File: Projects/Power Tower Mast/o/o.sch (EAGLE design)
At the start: 29 parts

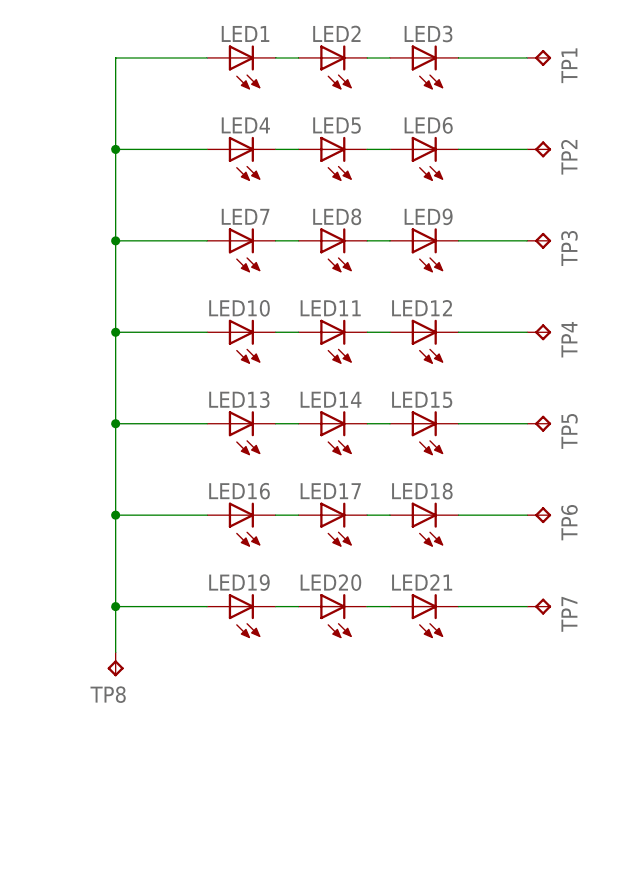
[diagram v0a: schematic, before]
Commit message: updated with extra vias and panelized
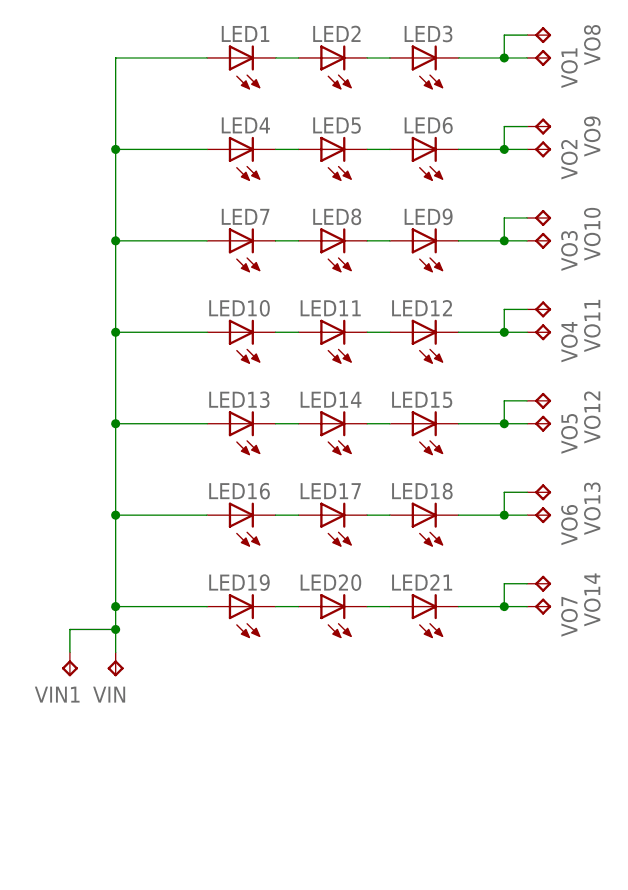
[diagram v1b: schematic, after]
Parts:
- added VIN1, VO10, VO11, VO12, VO13, VO14, VO8, VO9: (no value), CyberRailGuru:TEST_POINTPAD1-20
- renumbered TP1 to VO1, TP2 to VO2, TP3 to VO3, TP4 to VO4, TP5 to VO5, TP6 to VO6, TP7 to VO7, TP8 to VIN
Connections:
- removed net VIN2: LED1.A, LED10.A, LED13.A, LED16.A, LED19.A, LED4.A, LED7.A, VIN.TP
- removed net VOUT10: LED12.C, VO4.TP
- removed net VOUT11: LED15.C, VO5.TP
- removed net VOUT12: LED18.C, VO6.TP
- removed net VOUT13: LED21.C, VO7.TP
- removed net VOUT8: LED6.C, VO2.TP
- removed net VOUT9: LED9.C, VO3.TP
- new net VIN: LED1.A, LED10.A, LED13.A, LED16.A, LED19.A, LED4.A, LED7.A, VIN.TP, VIN1.TP
- new net VOUT1: LED3.C, VO1.TP, VO8.TP
- new net VOUT2: LED6.C, VO2.TP, VO9.TP
- new net VOUT3: LED9.C, VO10.TP, VO3.TP
- new net VOUT4: LED12.C, VO11.TP, VO4.TP
- new net VOUT5: LED15.C, VO12.TP, VO5.TP
- new net VOUT6: LED18.C, VO13.TP, VO6.TP
- net VOUT7: now also LED21.C, VO14.TP, VO7.TP; no longer LED3.C, VO1.TP

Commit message: fixed ratio for all letters; continued to update layouts
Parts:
- added LED22, LED23, LED24: (no value), CyberRailGuru:LED0805
- added VO15, VO16: (no value), CyberRailGuru:TEST_POINTPAD1-20
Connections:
- new net N$1: LED22.C, LED23.A
- new net N$2: LED23.C, LED24.A
- new net N$5: LED24.C, VO16.TP, VO8.TP
- net VIN: now also LED22.A
- net VOUT1: now also VO9.TP; no longer VO8.TP
- net VOUT2: now also VO10.TP; no longer VO9.TP
- net VOUT3: now also VO11.TP; no longer VO10.TP
- net VOUT4: now also VO12.TP; no longer VO11.TP
- net VOUT5: now also VO13.TP; no longer VO12.TP
- net VOUT6: now also VO14.TP; no longer VO13.TP
- net VOUT7: now also VO15.TP; no longer VO14.TP
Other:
- moved on the sheet: VIN, VIN1, VO10, VO11, VO12, VO13, VO14, VO8, VO9
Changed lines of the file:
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@@
 <part name="VO7" library="CyberRailGuru" deviceset="TEST_POINT" device="PAD1-20"/>
 <part name="VIN1" library="CyberRailGuru" deviceset="TEST_POINT" device="PAD1-20"/>
-<part name="VO8" library="CyberRailGuru" deviceset="TEST_POINT" device="PAD1-20"/>
 <part name="VO9" library="CyberRailGuru" deviceset="TEST_POINT" device="PAD1-20"/>
 <part name="VO10" library="CyberRailGuru" deviceset="TEST_POINT" device="PAD1-20"/>
@@
 <part name="VO13" library="CyberRailGuru" deviceset="TEST_POINT" device="PAD1-20"/>
 <part name="VO14" library="CyberRailGuru" deviceset="TEST_POINT" device="PAD1-20"/>
+<part name="VO15" library="CyberRailGuru" deviceset="TEST_POINT" device="PAD1-20"/>
+<part name="LED22" library="CyberRailGuru" deviceset="LED" device="0805"/>
+<part name="LED23" library="CyberRailGuru" deviceset="LED" device="0805"/>
+<part name="LED24" library="CyberRailGuru" deviceset="LED" device="0805"/>
+<part name="VO8" library="CyberRailGuru" deviceset="TEST_POINT" device="PAD1-20"/>
+<part name="VO16" library="CyberRailGuru" deviceset="TEST_POINT" device="PAD1-20"/>
 </parts>
 <sheets>
@@
 <instance part="LED20" gate="G$1" x="68.58" y="177.8" rot="R90"/>
 <instance part="LED19" gate="G$1" x="58.42" y="177.8" rot="R90"/>
-<instance part="VIN" gate="G$1" x="45.72" y="170.18" rot="R180"/>
+<instance part="VIN" gate="G$1" x="45.72" y="152.4" rot="R180"/>
 <instance part="VO1" gate="G$1" x="93.98" y="238.76" smashed="yes" rot="R270">
 <attribute name="NAME" x="95.25" y="240.03" size="1.778" layer="95" rot="R270"/>
@@
 <attribute name="VALUE" x="92.71" y="176.53" size="1.778" layer="96" rot="R270"/>
 </instance>
-<instance part="VIN1" gate="G$1" x="40.64" y="170.18" rot="R180"/>
-<instance part="VO8" gate="G$1" x="93.98" y="241.3" smashed="yes" rot="R270">
+<instance part="VIN1" gate="G$1" x="40.64" y="152.4" rot="R180"/>
+<instance part="VO9" gate="G$1" x="93.98" y="241.3" smashed="yes" rot="R270">
 <attribute name="NAME" x="97.79" y="242.57" size="1.778" layer="95" rot="R270"/>
 <attribute name="VALUE" x="92.71" y="240.03" size="1.778" layer="96" rot="R270"/>
 </instance>
-<instance part="VO9" gate="G$1" x="93.98" y="231.14" smashed="yes" rot="R270">
+<instance part="VO10" gate="G$1" x="93.98" y="231.14" smashed="yes" rot="R270">
 <attribute name="NAME" x="97.79" y="232.41" size="1.778" layer="95" rot="R270"/>
 <attribute name="VALUE" x="92.71" y="229.87" size="1.778" layer="96" rot="R270"/>
 </instance>
-<instance part="VO10" gate="G$1" x="93.98" y="220.98" smashed="yes" rot="R270">
+<instance part="VO11" gate="G$1" x="93.98" y="220.98" smashed="yes" rot="R270">
 <attribute name="NAME" x="97.79" y="222.25" size="1.778" layer="95" rot="R270"/>
 <attribute name="VALUE" x="92.71" y="219.71" size="1.778" layer="96" rot="R270"/>
 </instance>
-<instance part="VO11" gate="G$1" x="93.98" y="210.82" smashed="yes" rot="R270">
+<instance part="VO12" gate="G$1" x="93.98" y="210.82" smashed="yes" rot="R270">
 <attribute name="NAME" x="97.79" y="212.09" size="1.778" layer="95" rot="R270"/>
 <attribute name="VALUE" x="92.71" y="209.55" size="1.778" layer="96" rot="R270"/>
 </instance>
-<instance part="VO12" gate="G$1" x="93.98" y="200.66" smashed="yes" rot="R270">
+<instance part="VO13" gate="G$1" x="93.98" y="200.66" smashed="yes" rot="R270">
 <attribute name="NAME" x="97.79" y="201.93" size="1.778" layer="95" rot="R270"/>
 <attribute name="VALUE" x="92.71" y="199.39" size="1.778" layer="96" rot="R270"/>
 </instance>
-<instance part="VO13" gate="G$1" x="93.98" y="190.5" smashed="yes" rot="R270">
+<instance part="VO14" gate="G$1" x="93.98" y="190.5" smashed="yes" rot="R270">
 <attribute name="NAME" x="97.79" y="191.77" size="1.778" layer="95" rot="R270"/>
 <attribute name="VALUE" x="92.71" y="189.23" size="1.778" layer="96" rot="R270"/>
 </instance>
-<instance part="VO14" gate="G$1" x="93.98" y="180.34" smashed="yes" rot="R270">
+<instance part="VO15" gate="G$1" x="93.98" y="180.34" smashed="yes" rot="R270">
 <attribute name="NAME" x="97.79" y="181.61" size="1.778" layer="95" rot="R270"/>
 <attribute name="VALUE" x="92.71" y="179.07" size="1.778" layer="96" rot="R270"/>
+</instance>
+<instance part="LED22" gate="G$1" x="58.42" y="167.64" rot="R90"/>
+<instance part="LED23" gate="G$1" x="68.58" y="167.64" rot="R90"/>
+<instance part="LED24" gate="G$1" x="78.74" y="167.64" rot="R90"/>
+<instance part="VO8" gate="G$1" x="93.98" y="167.64" smashed="yes" rot="R270">
+<attribute name="NAME" x="95.25" y="168.91" size="1.778" layer="95" rot="R270"/>
+<attribute name="VALUE" x="92.71" y="166.37" size="1.778" layer="96" rot="R270"/>
+</instance>
+<instance part="VO16" gate="G$1" x="93.98" y="170.18" smashed="yes" rot="R270">
+<attribute name="NAME" x="97.79" y="171.45" size="1.778" layer="95" rot="R270"/>
+<attribute name="VALUE" x="92.71" y="168.91" size="1.778" layer="96" rot="R270"/>
 </instance>
 </instances>
@@
 <wire x1="83.82" y1="238.76" x2="88.9" y2="238.76" width="0.1524" layer="91"/>
 <pinref part="VO1" gate="G$1" pin="TP"/>
-<pinref part="VO8" gate="G$1" pin="TP"/>
+<pinref part="VO9" gate="G$1" pin="TP"/>
 <wire x1="88.9" y1="238.76" x2="91.44" y2="238.76" width="0.1524" layer="91"/>
 <wire x1="91.44" y1="241.3" x2="88.9" y2="241.3" width="0.1524" layer="91"/>
@@
 <wire x1="83.82" y1="228.6" x2="88.9" y2="228.6" width="0.1524" layer="91"/>
 <pinref part="VO2" gate="G$1" pin="TP"/>
-<pinref part="VO9" gate="G$1" pin="TP"/>
+<pinref part="VO10" gate="G$1" pin="TP"/>
 <wire x1="88.9" y1="228.6" x2="91.44" y2="228.6" width="0.1524" layer="91"/>
 <wire x1="91.44" y1="231.14" x2="88.9" y2="231.14" width="0.1524" layer="91"/>
@@
 <wire x1="83.82" y1="218.44" x2="88.9" y2="218.44" width="0.1524" layer="91"/>
 <pinref part="VO3" gate="G$1" pin="TP"/>
-<pinref part="VO10" gate="G$1" pin="TP"/>
+<pinref part="VO11" gate="G$1" pin="TP"/>
 <wire x1="88.9" y1="218.44" x2="91.44" y2="218.44" width="0.1524" layer="91"/>
 <wire x1="91.44" y1="220.98" x2="88.9" y2="220.98" width="0.1524" layer="91"/>
@@
 <wire x1="83.82" y1="208.28" x2="88.9" y2="208.28" width="0.1524" layer="91"/>
 <pinref part="VO4" gate="G$1" pin="TP"/>
-<pinref part="VO11" gate="G$1" pin="TP"/>
+<pinref part="VO12" gate="G$1" pin="TP"/>
 <wire x1="88.9" y1="208.28" x2="91.44" y2="208.28" width="0.1524" layer="91"/>
 <wire x1="91.44" y1="210.82" x2="88.9" y2="210.82" width="0.1524" layer="91"/>
@@
 <wire x1="83.82" y1="198.12" x2="88.9" y2="198.12" width="0.1524" layer="91"/>
 <pinref part="VO5" gate="G$1" pin="TP"/>
-<pinref part="VO12" gate="G$1" pin="TP"/>
+<pinref part="VO13" gate="G$1" pin="TP"/>
 <wire x1="88.9" y1="198.12" x2="91.44" y2="198.12" width="0.1524" layer="91"/>
 <wire x1="91.44" y1="200.66" x2="88.9" y2="200.66" width="0.1524" layer="91"/>
@@
 <wire x1="83.82" y1="187.96" x2="88.9" y2="187.96" width="0.1524" layer="91"/>
 <pinref part="VO6" gate="G$1" pin="TP"/>
-<pinref part="VO13" gate="G$1" pin="TP"/>
+<pinref part="VO14" gate="G$1" pin="TP"/>
 <wire x1="88.9" y1="187.96" x2="91.44" y2="187.96" width="0.1524" layer="91"/>
 <wire x1="91.44" y1="190.5" x2="88.9" y2="190.5" width="0.1524" layer="91"/>
@@
 <wire x1="83.82" y1="177.8" x2="88.9" y2="177.8" width="0.1524" layer="91"/>
 <pinref part="VO7" gate="G$1" pin="TP"/>
-<pinref part="VO14" gate="G$1" pin="TP"/>
+<pinref part="VO15" gate="G$1" pin="TP"/>
 <wire x1="88.9" y1="177.8" x2="91.44" y2="177.8" width="0.1524" layer="91"/>
 <wire x1="91.44" y1="180.34" x2="88.9" y2="180.34" width="0.1524" layer="91"/>
@@
 <wire x1="45.72" y1="198.12" x2="45.72" y2="187.96" width="0.1524" layer="91"/>
 <wire x1="45.72" y1="187.96" x2="45.72" y2="177.8" width="0.1524" layer="91"/>
-<wire x1="45.72" y1="177.8" x2="45.72" y2="175.26" width="0.1524" layer="91"/>
-<wire x1="45.72" y1="175.26" x2="45.72" y2="172.72" width="0.1524" layer="91"/>
+<wire x1="45.72" y1="177.8" x2="45.72" y2="167.64" width="0.1524" layer="91"/>
+<wire x1="45.72" y1="167.64" x2="45.72" y2="157.48" width="0.1524" layer="91"/>
+<wire x1="45.72" y1="157.48" x2="45.72" y2="154.94" width="0.1524" layer="91"/>
 <wire x1="55.88" y1="177.8" x2="45.72" y2="177.8" width="0.1524" layer="91"/>
 <pinref part="LED16" gate="G$1" pin="A"/>
@@
 <pinref part="VIN" gate="G$1" pin="TP"/>
 <pinref part="VIN1" gate="G$1" pin="TP"/>
-<wire x1="40.64" y1="172.72" x2="40.64" y2="175.26" width="0.1524" layer="91"/>
-<wire x1="40.64" y1="175.26" x2="45.72" y2="175.26" width="0.1524" layer="91"/>
-<junction x="45.72" y="175.26"/>
-</segment>
-</net>
+<wire x1="40.64" y1="154.94" x2="40.64" y2="157.48" width="0.1524" layer="91"/>
+<wire x1="40.64" y1="157.48" x2="45.72" y2="157.48" width="0.1524" layer="91"/>
+<junction x="45.72" y="157.48"/>
+<pinref part="LED22" gate="G$1" pin="A"/>
+<wire x1="55.88" y1="167.64" x2="45.72" y2="167.64" width="0.1524" layer="91"/>
+<junction x="45.72" y="167.64"/>
+</segment>
+</net>
+<net name="N$1" class="0">
+<segment>
+<pinref part="LED23" gate="G$1" pin="A"/>
+<pinref part="LED22" gate="G$1" pin="C"/>
+<wire x1="66.04" y1="167.64" x2="63.5" y2="167.64" width="0.1524" layer="91"/>
+</segment>
+</net>
+<net name="N$2" class="0">
+<segment>
+<pinref part="LED24" gate="G$1" pin="A"/>
+<pinref part="LED23" gate="G$1" pin="C"/>
+<wire x1="76.2" y1="167.64" x2="73.66" y2="167.64" width="0.1524" layer="91"/>
+</segment>
+</net>
+<net name="N$5" class="0">
+<segment>
+<pinref part="VO8" gate="G$1" pin="TP"/>
+<pinref part="LED24" gate="G$1" pin="C"/>
+<wire x1="91.44" y1="167.64" x2="88.9" y2="167.64" width="0.1524" layer="91"/>
+<pinref part="VO16" gate="G$1" pin="TP"/>
+<wire x1="88.9" y1="167.64" x2="83.82" y2="167.64" width="0.1524" layer="91"/>
+<wire x1="91.44" y1="170.18" x2="88.9" y2="170.18" width="0.1524" layer="91"/>
+<wire x1="88.9" y1="170.18" x2="88.9" y2="167.64" width="0.1524" layer="91"/>
+<junction x="88.9" y="167.64"/>
+</segment>
+</net>
